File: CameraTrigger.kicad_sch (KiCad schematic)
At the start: 13 parts, among them U1 MAX4466EXK_T

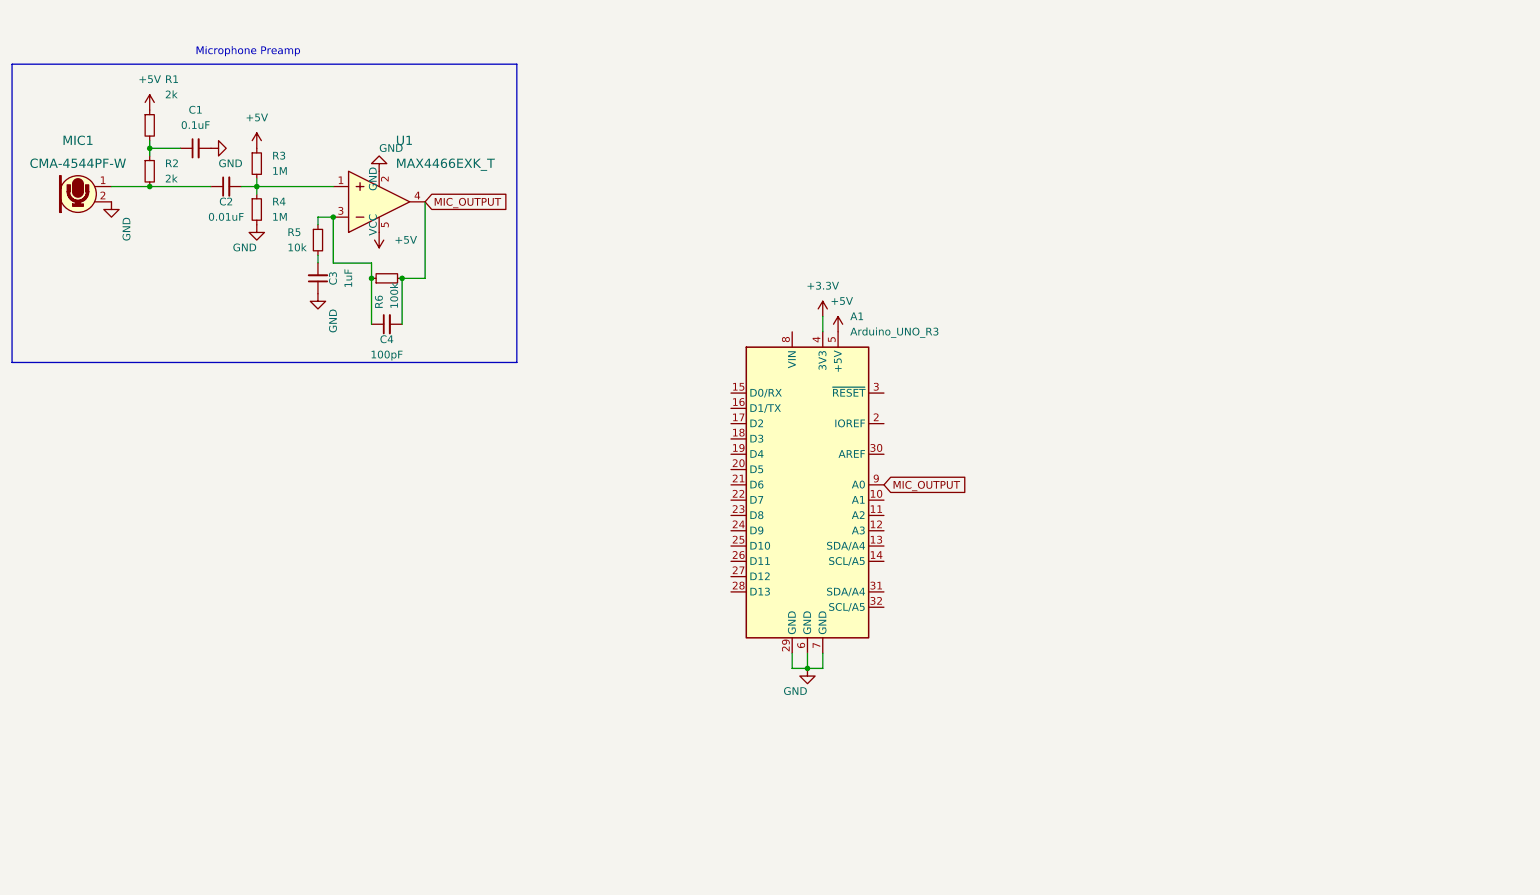
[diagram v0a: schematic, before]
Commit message: Add final sensors and triggering mechanisms
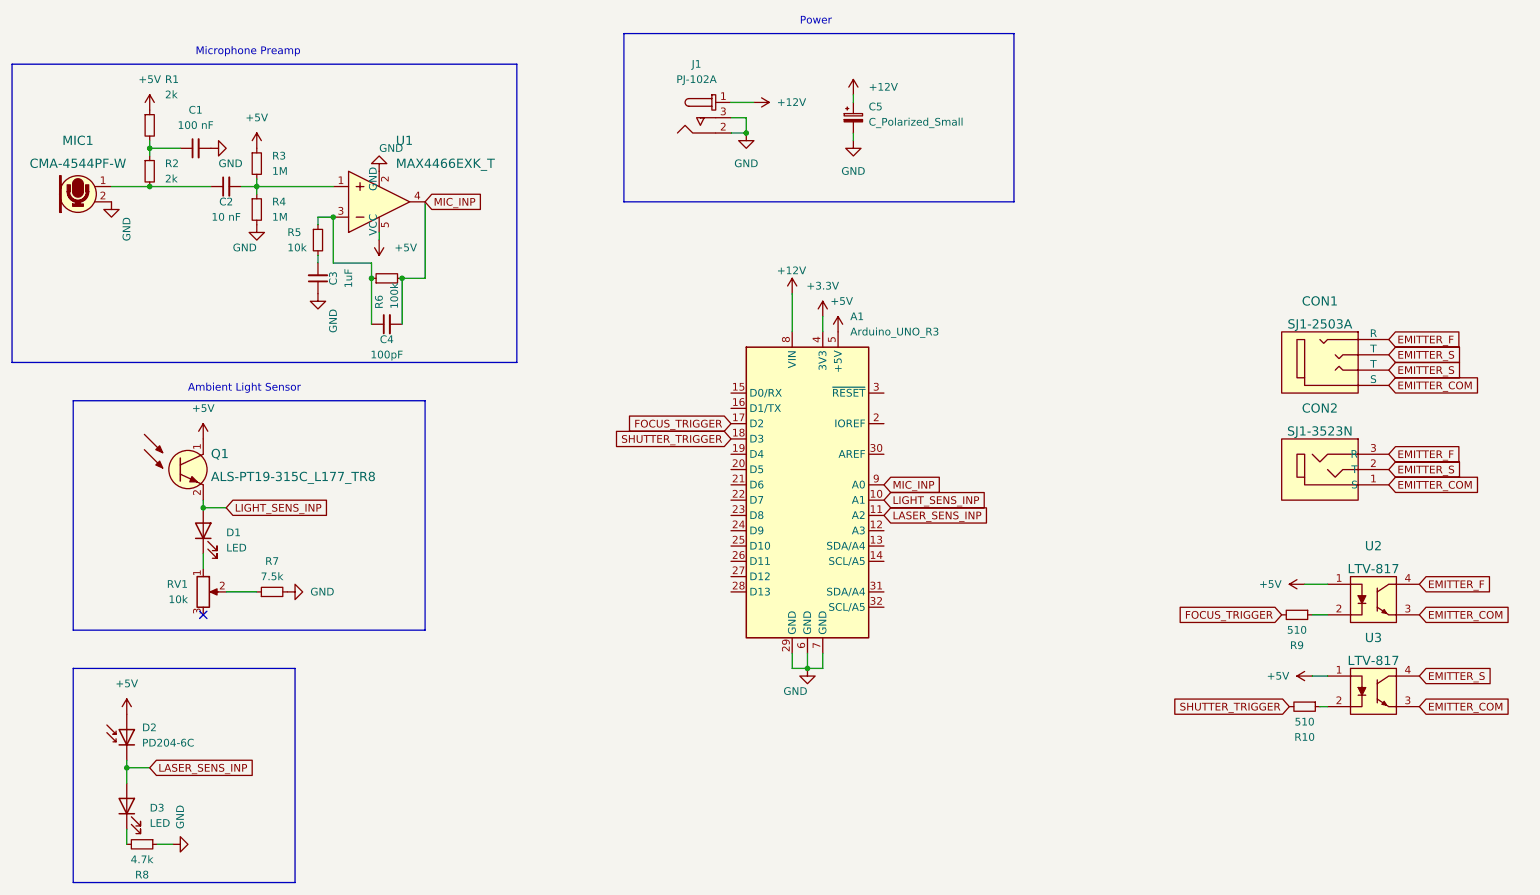
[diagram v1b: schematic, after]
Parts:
- added C5: C_Polarized_Small, Capacitor_Tantalum_SMD:CP_EIA-3528-15_AVX-H, symbol Device:C_Polarized_Small
- added CON1: SJ1-2503A, digikey-footprints:Headphone_Jack_2.5mm_SJ1-2503A, symbol dk_Barrel-Audio-Connectors:SJ1-2503A
- added CON2: SJ1-3523N, digikey-footprints:Headphone_Jack_3.5mm_SJ1-3523N, symbol dk_Barrel-Audio-Connectors:SJ1-3523N
- added D1, D3: LED, LED_THT:LED_D3.0mm, symbol Device:LED
- added D2: PD204-6C, LED_THT:LED_D3.0mm, symbol Device:D_Photo
- added J1: PJ-102A, digikey-footprints:Barrel_Jack_5.5mmODx2.1mmID_PJ-102A, symbol dk_Barrel-Power-Connectors:PJ-102A
- added Q1: ALS-PT19-315C_L177_TR8, digikey-footprints:LED_2-SMD_No_Lead_1.7x0.8mm, symbol dk_Optical-Sensors-Phototransistors:ALS-PT19-315C_L177_TR8
- added R10, R9: 510, Resistor_SMD:R_0805_2012Metric, symbol Device:R_Small
- added R7: 7.5k, Resistor_SMD:R_0805_2012Metric, symbol Device:R_Small
- added R8: 4.7k, Resistor_SMD:R_0805_2012Metric, symbol Device:R_Small
- added RV1: 10k, Potentiometer_THT:Potentiometer_Piher_PT-10-V10_Vertical, symbol Device:R_Potentiometer
- added U2, U3: LTV-817, digikey-footprints:DIP-4_W7.62mm, symbol dk_Optoisolators-Transistor-Photovoltaic-Output:LTV-817
- C1: value 0.1uF -> 100 nF; footprint (none) -> Capacitor_SMD:C_0805_2012Metric; LCSC (none) -> C28233
- C2: value 0.01uF -> 10 nF; footprint (none) -> Capacitor_SMD:C_0805_2012Metric; LCSC (none) -> C1710
- C3: footprint (none) -> Capacitor_SMD:C_0805_2012Metric; LCSC (none) -> C28323
- C4: footprint (none) -> Capacitor_SMD:C_0805_2012Metric; LCSC (none) -> C1790
- R1, R2: footprint (none) -> Resistor_SMD:R_0805_2012Metric; LCSC (none) -> C17604
- R3, R4: footprint (none) -> Resistor_SMD:R_0805_2012Metric; LCSC (none) -> C17514
- R5: footprint (none) -> Resistor_SMD:R_0805_2012Metric; LCSC (none) -> C17414
- R6: footprint (none) -> Resistor_SMD:R_0805_2012Metric; LCSC (none) -> C149504
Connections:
- net +5V: now also D2.2 (A), Q1.1 (C), U2.1, U3.1
- net GND: now also C5.2, J1.2, J1.3, R7.2, R8.1
- net LIGHT_SENS_INP: now reaches A1.10 (A1)
- net LIGHT_SENS_INP: now also D1.2 (A), Q1.2 (E)
- net LASER_SENS_INP: now reaches A1.11 (A2)
- net LASER_SENS_INP: now also D2.1 (K), D3.2 (A)
- net FOCUS_TRIGGER: now reaches A1.17 (D2)
- net FOCUS_TRIGGER: now also R9.2
- net SHUTTER_TRIGGER: now reaches A1.18 (D3)
- net SHUTTER_TRIGGER: now also R10.2
- net +12V: now reaches A1.8 (VIN)
- net +12V: now also C5.1, J1.1
- net MIC_OUTPUT renamed MIC_INP
- new net: D3.1 (K), R8.2
- new net: R9.1, U2.2
- new net: R7.1, RV1.2
- new net: R10.1, U3.2
- new net: D1.1 (K), RV1.1
- new net EMITTER_COM: CON1.1 (S), CON2.1 (S), U2.3, U3.3
- new net EMITTER_F: CON1.4 (R), CON2.3 (R), U2.4
- new net EMITTER_S: CON1.2 (T), CON1.3 (T), CON2.2 (T), U3.4
- no-connect marks 0 -> 1
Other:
- note added: "Ambient Light Sensor"
- note added: "Power"
